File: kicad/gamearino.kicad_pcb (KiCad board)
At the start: 2 copper layers, 60 x 56 mm, 60 parts, among them Q1 PMBT3904,215, Q2 PMBT3904,215, SW1 Left, SW2 Up, SW3 Down, SW4 Right, SW5 Select, SW6 Start, SW7 B, SW8 A, U1 ESP-12F, U2 CH340C, U3 AMS1117-3.3, U4 QG-2864KSWEG01, X1 USB-C/16p

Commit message: wip
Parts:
- removed C12: 1u, Capacitor_SMD:C_0603_1608Metric
- removed D2: LED_Dual_green-red, htl_smd:LED_LiteOn_LTST-C195KGJRKT
- removed FID1, FID2: Fiducial, htl_mechanical:paste-fiducial
- removed the R10 at (137.2, 91.7)
- removed R20: 4k7, Resistor_SMD:R_0603_1608Metric
- removed the R9 at (123.5, 92.0)
- C10: value 10u/16V/X5R -> 4u7
- C11: value 1u -> 2u2; footprint Capacitor_SMD:C_0603_1608Metric -> Capacitor_SMD:C_0805_2012Metric
- D1: value BAV99 -> 1N4148
- Item1, Item2: footprint gamearino:ABKnopf_v2 -> gamearino:ABKnopf
- Item3, Item4: footprint gamearino:StartSelect_v2 -> gamearino:StartSelect
- Item5: footprint gamearino:Steuerkreuz_zeik_v2 -> gamearino:Steuerkreuz_zeik
- moved C10 0.25 mm to (140.8, 58.5)
- turned D1 to 180 degrees
- renumbered X1 to J1, R12 to R10, R13 to R11, R14 to R12, R15 to R13, R16 to R14, R17 to R15, R18 to R16, R19 to R17, R11 to R9
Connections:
- net /EN renamed Net-(R1-Pad2)
- D1 pad 1: Net-(C5-Pad1) -> Net-(D1-Pad1)
- D1 pad 2: (no net) -> Net-(C5-Pad1)
- D1 pad 3: Net-(D1-Pad3) -> (no net)
- J1 pad A5: Net-(R9-Pad2) -> (no net)
- J1 pad B5: Net-(R10-Pad1) (its old number) -> (no net)
- R12 pad 2: Net-(D1-Pad3) -> Net-(D1-Pad1)
- R14 pad 2: Net-(D1-Pad3) -> Net-(D1-Pad1)
- U2 pad 10: GND -> (no net)
- U2 pad 11: GND -> (no net)
- U2 pad 12: GND -> (no net)
- U2 pad 9: GND -> (no net)
- U4 pad 11: Net-(D1-Pad3) -> Net-(D1-Pad1)
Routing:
- net Net-(D1-Pad3): track 25.4 -> 0.00 mm, vias 2 -> 0
- net Net-(D1-Pad1): track 0.00 -> 24.8 mm, vias 0 -> 2
- net Net-(C3-Pad1): track 71.6 -> 55.1 mm, vias 4 -> 2
- net /Buttons/C0: track 97.1 -> 84.4 mm, vias 6 -> 2
- net /Buttons/R2: track 46.1 -> 34.2 mm, vias 6 -> 2
- net /Buttons/R1: track 158.9 -> 147.1 mm, vias 8 -> 6
- net GND: track 109.2 -> 99.1 mm, vias 50 -> 24
- net Net-(D2-Pad2): track 9.16 -> 0.00 mm
- net /Buttons/R0: track 163.5 -> 154.5 mm
- net Net-(R10-Pad1) (its old number): track 8.25 -> 0.00 mm
- net Net-(R9-Pad2): track 8.19 -> 0.00 mm
- net /Buttons/C1: track 89.5 -> 83.5 mm, vias 6 -> 4
- net /Buttons/C2: track 40.3 -> 34.3 mm
- net /USB/D-: track 21.2 -> 23.9 mm
- net Net-(C6-Pad1): track 20.1 -> 17.7 mm
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- removed copper zone on B.Cu, net +3V3
- removed copper zone on F.Cu, net +3V3
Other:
- net class Default: clearance 0.15 -> 0.25; trace_width 0.15 -> 0.25
- rule trace_clearance: 0.15 -> 0.25
- rule trace_min: 0.15 -> 0.2
- board text added: "Gamearino v0.0.1"
- board text removed: "A"
- board text removed: "AMS1117-3.3"
- board text removed: "B"
- board text removed: "CH340C"
- board text removed: "DOWN"
- board text removed: "ESP-12F (ESP8266) Arduino IDE settings compatible with NodeMCU V1.0"
- board text removed: "Gamearino V0.0.2"
- board text removed: "HTL STEYR 2021"
- board text removed: "LEFT"
- board text removed: "RIGHT"
- board text removed: "SELECT"
- board text removed: "START"
- board text removed: "UP"
- board text removed: "V0.0.2"
- board text removed: "github.com/KarlZeilhofer/gamearino"

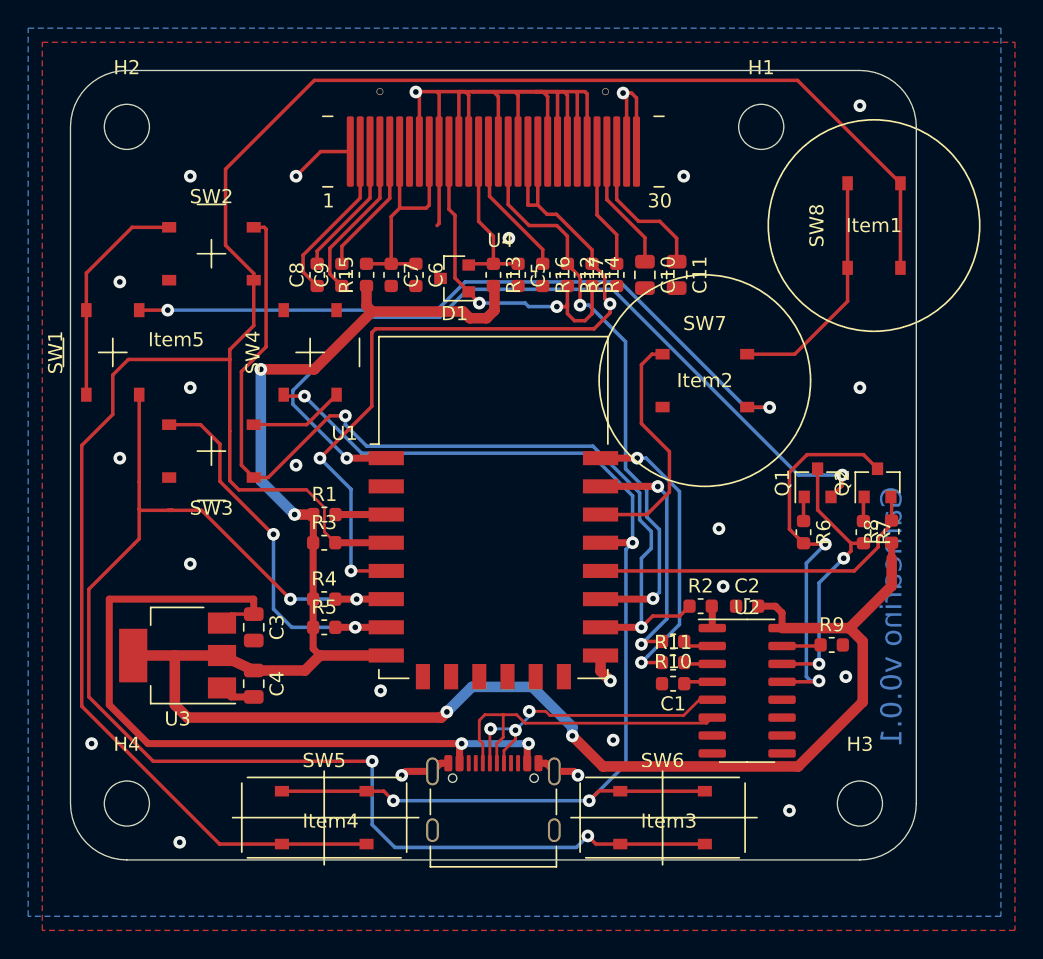
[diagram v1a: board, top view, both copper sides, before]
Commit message: PCB v0.0.2 wieder hergestellt
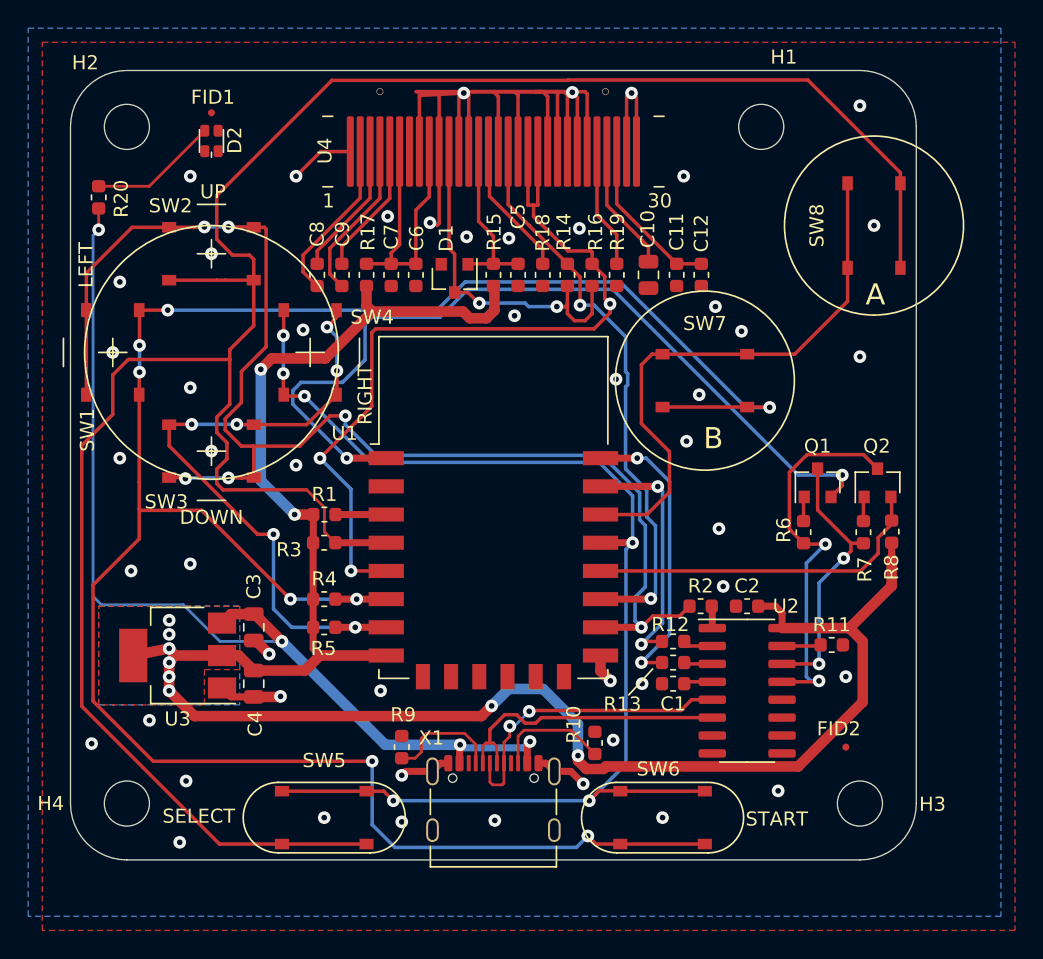
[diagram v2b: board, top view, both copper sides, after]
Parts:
- added C12: 1u, Capacitor_SMD:C_0603_1608Metric, F.Cu at (144.8, 58.5)
- added D2: LED_Dual_green-red, htl_smd:LED_LiteOn_LTST-C195KGJRKT, F.Cu at (110.0, 49.0)
- added FID1: Fiducial, htl_mechanical:paste-fiducial, F.Cu at (110.0, 47.0)
- added FID2: Fiducial, htl_mechanical:paste-fiducial, F.Cu at (155.0, 92.0)
- added R10: 5k1, Resistor_SMD:R_0603_1608Metric, F.Cu at (137.2, 91.7)
- added R20: 4k7, Resistor_SMD:R_0603_1608Metric, F.Cu at (102.0, 53.0)
- added R9: 5k1, Resistor_SMD:R_0603_1608Metric, F.Cu at (123.5, 92.0)
- C10: value 4u7 -> 10u/16V/X5R
- C11: value 2u2 -> 1u; footprint Capacitor_SMD:C_0805_2012Metric -> Capacitor_SMD:C_0603_1608Metric
- D1: value 1N4148 -> BAV99
- Item1, Item2: footprint gamearino:ABKnopf -> gamearino:ABKnopf_v2
- Item3, Item4: footprint gamearino:StartSelect -> gamearino:StartSelect_v2
- Item5: footprint gamearino:Steuerkreuz_zeik -> gamearino:Steuerkreuz_zeik_v2
- moved C10 0.25 mm to (141.0, 58.5)
- turned D1 to 270 degrees
- renumbered R9 to R11, R10 to R12, R11 to R13, R12 to R14, R13 to R15, R14 to R16, R15 to R17, R16 to R18, R17 to R19, J1 to X1
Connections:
- net Net-(R1-Pad2) renamed /EN
- D1 pad 1: Net-(D1-Pad1) -> Net-(C5-Pad1)
- D1 pad 2: Net-(C5-Pad1) -> (no net)
- D1 pad 3: (no net) -> Net-(D1-Pad3)
- R14 pad 2: Net-(D1-Pad1) -> Net-(D1-Pad3)
- R16 pad 2: Net-(D1-Pad1) -> Net-(D1-Pad3)
- U2 pad 10: (no net) -> GND
- U2 pad 11: (no net) -> GND
- U2 pad 12: (no net) -> GND
- U2 pad 9: (no net) -> GND
- U4 pad 11: Net-(D1-Pad1) -> Net-(D1-Pad3)
- X1 pad A5: (no net) -> Net-(R9-Pad2)
- X1 pad B5: (no net) -> Net-(R10-Pad1)
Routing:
- net Net-(D1-Pad3): track 0.00 -> 25.4 mm, vias 0 -> 2
- net Net-(D1-Pad1): track 24.8 -> 0.00 mm, vias 2 -> 0
- net Net-(C3-Pad1): track 55.1 -> 71.6 mm, vias 2 -> 4
- net /Buttons/C0: track 84.4 -> 97.1 mm, vias 2 -> 6
- net /Buttons/R2: track 34.2 -> 46.1 mm, vias 2 -> 6
- net /Buttons/R1: track 147.1 -> 158.9 mm, vias 6 -> 8
- net GND: track 99.1 -> 109.2 mm, vias 24 -> 50
- net Net-(D2-Pad2): track 0.00 -> 9.16 mm
- net /Buttons/R0: track 154.5 -> 163.5 mm
- net Net-(R10-Pad1): track 0.00 -> 8.25 mm
- net Net-(R9-Pad2): track 0.00 -> 8.19 mm
- net /Buttons/C1: track 83.5 -> 89.5 mm, vias 4 -> 6
- net /Buttons/C2: track 34.3 -> 40.3 mm
- net /USB/D-: track 23.9 -> 21.2 mm
- net Net-(C6-Pad1): track 17.7 -> 20.1 mm
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- added copper zone on B.Cu, net +3V3
- added copper zone on F.Cu, net +3V3
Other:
- net class Default: clearance 0.25 -> 0.15; trace_width 0.25 -> 0.15
- rule trace_clearance: 0.25 -> 0.15
- rule trace_min: 0.2 -> 0.15
- board text added: "A"
- board text added: "AMS1117-3.3"
- board text added: "B"
- board text added: "CH340C"
- board text added: "DOWN"
- board text added: "ESP-12F (ESP8266) Arduino IDE settings compatible with NodeMCU V1.0"
- board text added: "Gamearino V0.0.2"
- board text added: "HTL STEYR 2021"
- board text added: "LEFT"
- board text added: "RIGHT"
- board text added: "SELECT"
- board text added: "START"
- board text added: "UP"
- board text added: "V0.0.2"
- board text added: "github.com/KarlZeilhofer/gamearino"
- board text removed: "Gamearino v0.0.1"
